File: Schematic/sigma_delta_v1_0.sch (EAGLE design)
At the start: 30 parts, among them Q1 BS170, Q2 BS170

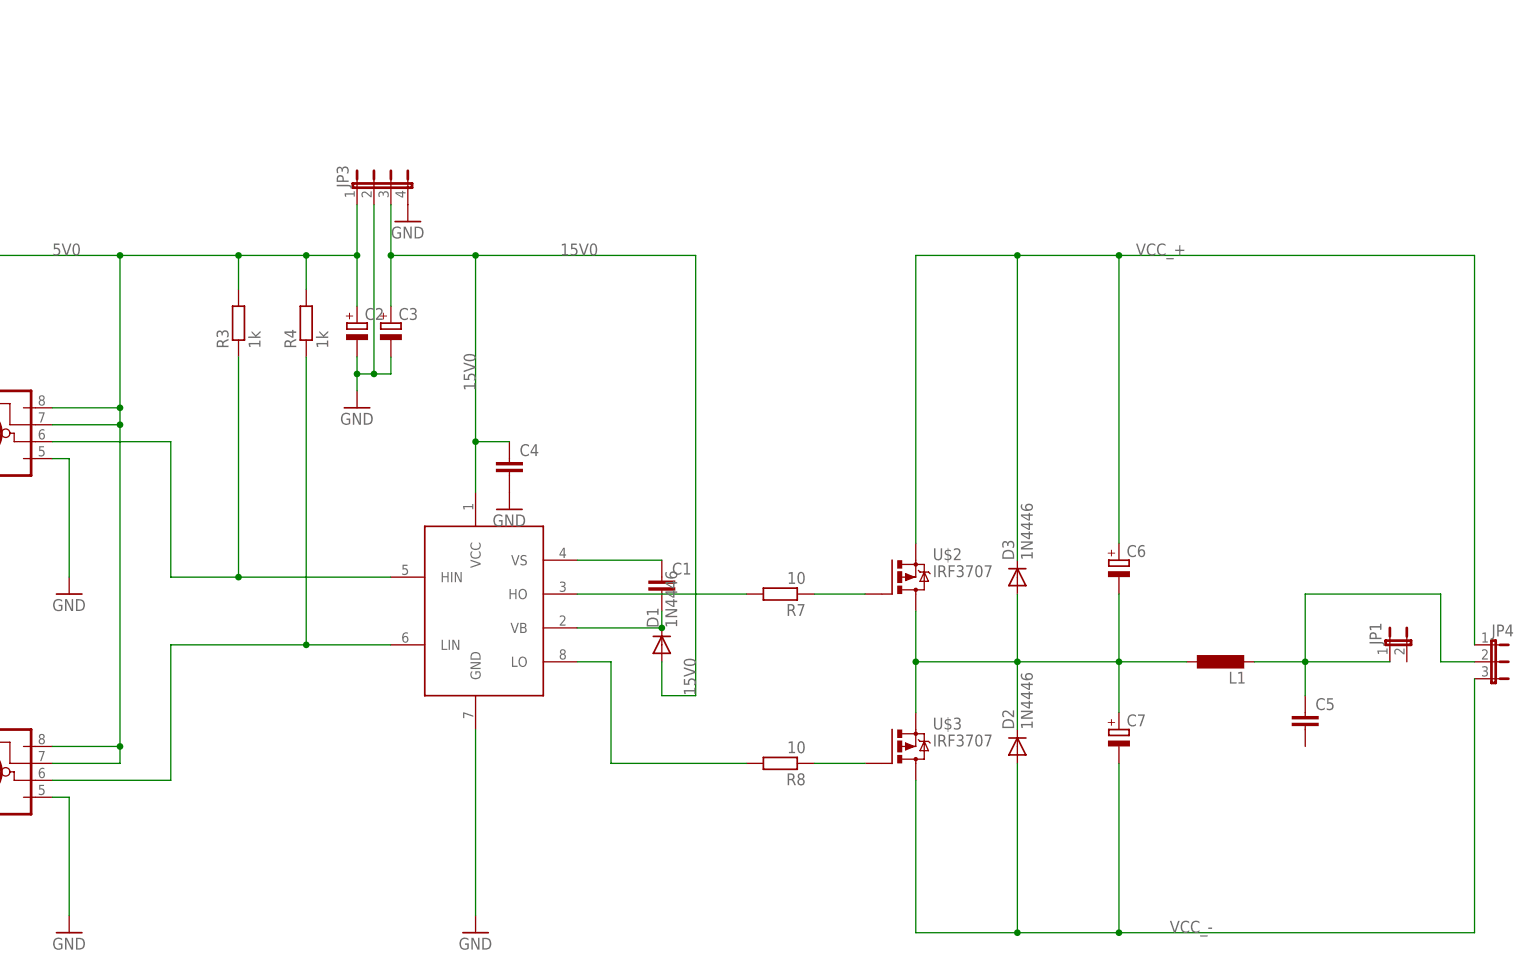
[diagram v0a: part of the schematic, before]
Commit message: first successfull stream of an audio file to the FPGA
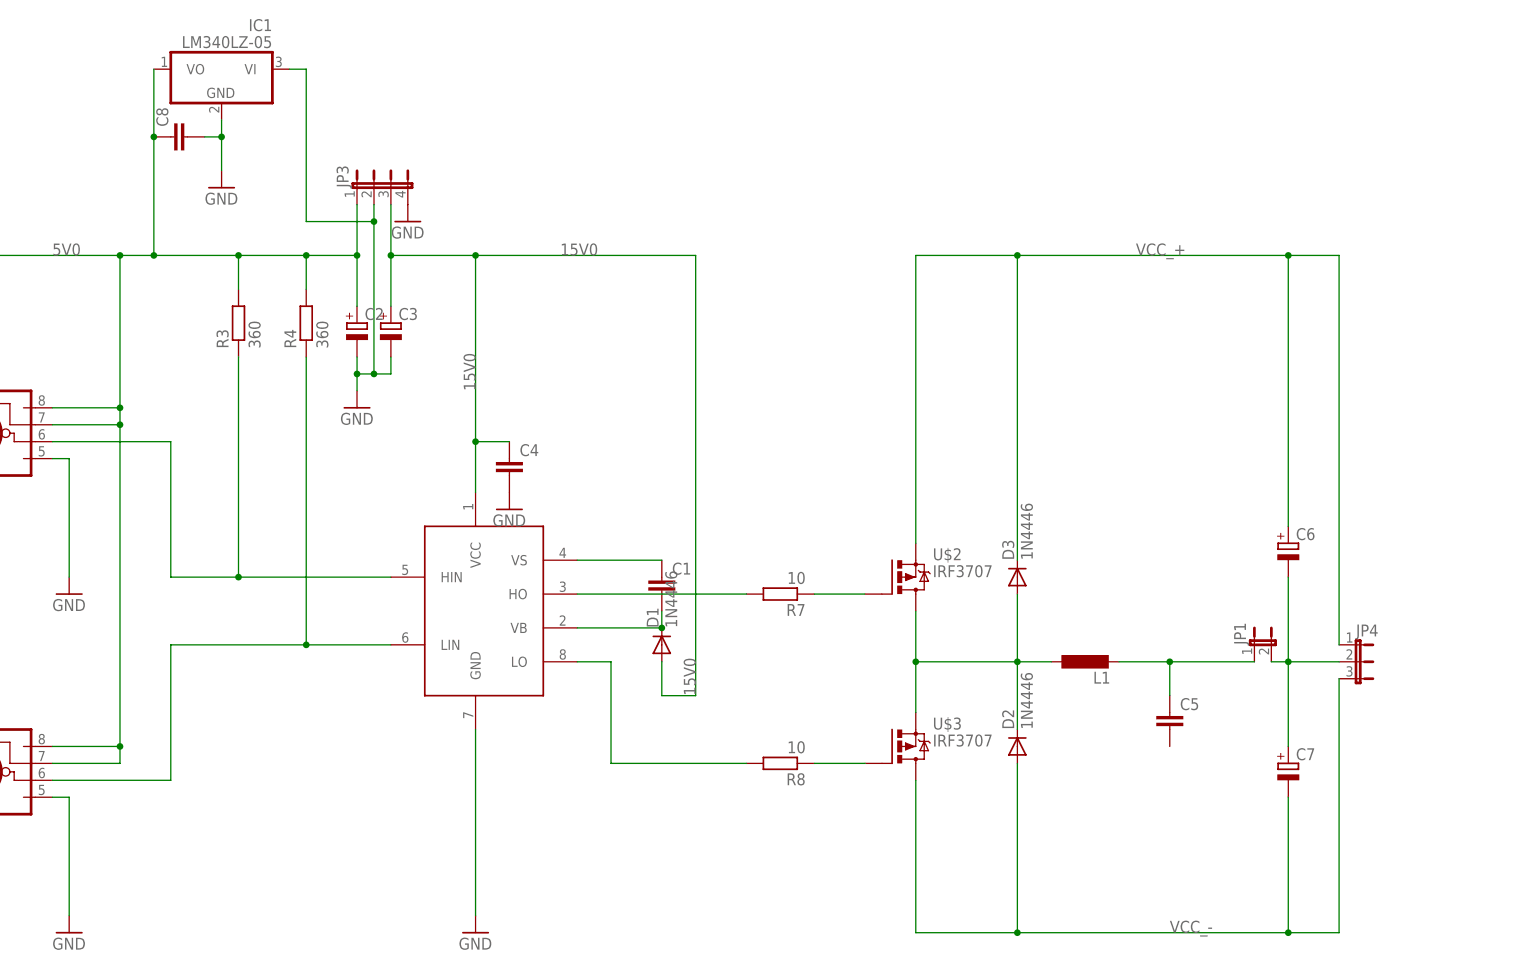
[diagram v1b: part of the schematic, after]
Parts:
- added C8: (no value), rcl:C-EU025-030X050
- added IC1: LM340LZ-05, linear:LM340LZ-05
- R3, R4: value 1k -> 360
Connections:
- new net N$19: C6.-, C7.+, JP1.2, JP4.2
- net 5V0: now also C8.1, IC1.VO
- net GND: now also C8.2, IC1.GND, IC1.VI
- net N$10: no longer JP4.2
- net N$9: no longer C6.-, C7.+
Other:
- moved on the sheet: C5, C6, C7, JP1, JP4, L1
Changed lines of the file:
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@@
 <part name="GND_5V0" library="supply1" deviceset="GND" device=""/>
 <part name="GND5" library="supply1" deviceset="GND" device=""/>
-<part name="R3" library="eagle-ltspice" deviceset="R" device="0207/10" value="1k"/>
-<part name="R4" library="eagle-ltspice" deviceset="R" device="0207/10" value="1k"/>
+<part name="R3" library="eagle-ltspice" deviceset="R" device="0207/10" value="360"/>
+<part name="R4" library="eagle-ltspice" deviceset="R" device="0207/10" value="360"/>
 <part name="GND6" library="supply1" deviceset="GND" device=""/>
 <part name="SUPPLY1" library="supply2" deviceset="GND" device="" value="F_GND"/>
@@
 <part name="D3" library="diode" deviceset="1N4446" device=""/>
 <part name="JP4" library="jumper" deviceset="JP2E" device=""/>
+<part name="IC1" library="linear" deviceset="LM340?-*" device="LZ" technology="05"/>
+<part name="GND4" library="supply1" deviceset="GND" device=""/>
+<part name="C8" library="rcl" deviceset="C-EU" device="025-030X050"/>
 </parts>
 <sheets>
@@
 <instance part="GND3" gate="1" x="147.32" y="182.88"/>
 <instance part="U$1" gate="G$1" x="147.32" y="167.64"/>
-<instance part="L1" gate="G$1" x="254" y="160.02" rot="R90"/>
-<instance part="C5" gate="G$1" x="266.7" y="152.4"/>
-<instance part="JP1" gate="A" x="279.4" y="162.56"/>
+<instance part="L1" gate="G$1" x="233.68" y="160.02" rot="R90"/>
+<instance part="C5" gate="G$1" x="246.38" y="152.4"/>
+<instance part="JP1" gate="A" x="259.08" y="162.56"/>
 <instance part="JP2" gate="G$1" x="20.32" y="175.26" rot="R90"/>
 <instance part="JP3" gate="G$1" x="127" y="231.14"/>
-<instance part="C6" gate="G$1" x="238.76" y="175.26"/>
-<instance part="C7" gate="G$1" x="238.76" y="149.86"/>
+<instance part="C6" gate="G$1" x="264.16" y="177.8"/>
+<instance part="C7" gate="G$1" x="264.16" y="144.78"/>
 <instance part="D2" gate="1" x="223.52" y="147.32" rot="R90"/>
 <instance part="D3" gate="1" x="223.52" y="172.72" rot="R90"/>
-<instance part="JP4" gate="1" x="294.64" y="160.02" rot="R270"/>
+<instance part="JP4" gate="1" x="274.32" y="160.02" rot="R270"/>
+<instance part="IC1" gate="A" x="104.14" y="248.92" rot="MR0"/>
+<instance part="GND4" gate="1" x="104.14" y="231.14"/>
+<instance part="C8" gate="G$1" x="96.52" y="238.76" rot="R90"/>
 </instances>
 <busses>
@@
 <wire x1="124.46" y1="200.66" x2="124.46" y2="203.2" width="0.1524" layer="91"/>
 <wire x1="124.46" y1="203.2" x2="124.46" y2="205.74" width="0.1524" layer="91"/>
-<wire x1="127" y1="228.6" x2="127" y2="203.2" width="0.1524" layer="91"/>
+<wire x1="127" y1="228.6" x2="127" y2="226.06" width="0.1524" layer="91"/>
+<wire x1="127" y1="226.06" x2="127" y2="203.2" width="0.1524" layer="91"/>
 <wire x1="127" y1="203.2" x2="124.46" y2="203.2" width="0.1524" layer="91"/>
 <junction x="124.46" y="203.2"/>
@@
 <junction x="127" y="203.2"/>
 <pinref part="JP3" gate="G$1" pin="2"/>
+<wire x1="127" y1="226.06" x2="116.84" y2="226.06" width="0.1524" layer="91"/>
+<wire x1="116.84" y1="226.06" x2="116.84" y2="248.92" width="0.1524" layer="91"/>
+<pinref part="IC1" gate="A" pin="VI"/>
+<wire x1="116.84" y1="248.92" x2="114.3" y2="248.92" width="0.1524" layer="91"/>
+<junction x="127" y="226.06"/>
 </segment>
 <segment>
@@
 <pinref part="GND2" gate="1" pin="GND"/>
 <pinref part="JP3" gate="G$1" pin="4"/>
+</segment>
+<segment>
+<pinref part="IC1" gate="A" pin="GND"/>
+<pinref part="GND4" gate="1" pin="GND"/>
+<wire x1="104.14" y1="233.68" x2="104.14" y2="238.76" width="0.1524" layer="91"/>
+<pinref part="C8" gate="G$1" pin="2"/>
+<wire x1="104.14" y1="238.76" x2="104.14" y2="241.3" width="0.1524" layer="91"/>
+<wire x1="101.6" y1="238.76" x2="104.14" y2="238.76" width="0.1524" layer="91"/>
+<junction x="104.14" y="238.76"/>
 </segment>
 </net>
@@
 <wire x1="48.26" y1="220.98" x2="55.88" y2="220.98" width="0.1524" layer="91"/>
 <wire x1="55.88" y1="220.98" x2="88.9" y2="220.98" width="0.1524" layer="91"/>
-<wire x1="88.9" y1="220.98" x2="106.68" y2="220.98" width="0.1524" layer="91"/>
+<wire x1="88.9" y1="220.98" x2="93.98" y2="220.98" width="0.1524" layer="91"/>
+<wire x1="93.98" y1="220.98" x2="106.68" y2="220.98" width="0.1524" layer="91"/>
 <wire x1="106.68" y1="220.98" x2="116.84" y2="220.98" width="0.1524" layer="91"/>
 <wire x1="116.84" y1="220.98" x2="116.84" y2="215.9" width="0.1524" layer="91"/>
@@
 <junction x="88.9" y="220.98"/>
 <pinref part="JP3" gate="G$1" pin="1"/>
+<pinref part="IC1" gate="A" pin="VO"/>
+<wire x1="93.98" y1="248.92" x2="93.98" y2="238.76" width="0.1524" layer="91"/>
+<junction x="93.98" y="220.98"/>
+<pinref part="C8" gate="G$1" pin="1"/>
+<wire x1="93.98" y1="238.76" x2="93.98" y2="220.98" width="0.1524" layer="91"/>
+<junction x="93.98" y="238.76"/>
 </segment>
 </net>
@@
 <pinref part="L1" gate="G$1" pin="1"/>
 <wire x1="208.28" y1="160.02" x2="208.28" y2="152.4" width="0.1524" layer="91"/>
-<wire x1="248.92" y1="160.02" x2="238.76" y2="160.02" width="0.1524" layer="91"/>
 <junction x="208.28" y="160.02"/>
-<pinref part="C6" gate="G$1" pin="-"/>
-<pinref part="C7" gate="G$1" pin="+"/>
-<wire x1="238.76" y1="160.02" x2="223.52" y2="160.02" width="0.1524" layer="91"/>
+<wire x1="228.6" y1="160.02" x2="223.52" y2="160.02" width="0.1524" layer="91"/>
 <wire x1="223.52" y1="160.02" x2="208.28" y2="160.02" width="0.1524" layer="91"/>
-<wire x1="238.76" y1="170.18" x2="238.76" y2="160.02" width="0.1524" layer="91"/>
-<junction x="238.76" y="160.02"/>
-<wire x1="238.76" y1="160.02" x2="238.76" y2="152.4" width="0.1524" layer="91"/>
 <pinref part="D2" gate="1" pin="C"/>
 <wire x1="223.52" y1="149.86" x2="223.52" y2="160.02" width="0.1524" layer="91"/>
@@
 <pinref part="L1" gate="G$1" pin="2"/>
 <pinref part="C5" gate="G$1" pin="1"/>
-<wire x1="259.08" y1="160.02" x2="266.7" y2="160.02" width="0.1524" layer="91"/>
-<wire x1="266.7" y1="160.02" x2="266.7" y2="154.94" width="0.1524" layer="91"/>
-<wire x1="266.7" y1="160.02" x2="279.4" y2="160.02" width="0.1524" layer="91"/>
+<wire x1="238.76" y1="160.02" x2="246.38" y2="160.02" width="0.1524" layer="91"/>
+<wire x1="246.38" y1="160.02" x2="246.38" y2="154.94" width="0.1524" layer="91"/>
+<wire x1="246.38" y1="160.02" x2="259.08" y2="160.02" width="0.1524" layer="91"/>
 <pinref part="JP1" gate="A" pin="1"/>
-<junction x="266.7" y="160.02"/>
-<wire x1="266.7" y1="160.02" x2="266.7" y2="170.18" width="0.1524" layer="91"/>
-<wire x1="266.7" y1="170.18" x2="287.02" y2="170.18" width="0.1524" layer="91"/>
-<wire x1="287.02" y1="170.18" x2="287.02" y2="160.02" width="0.1524" layer="91"/>
-<pinref part="JP4" gate="1" pin="2"/>
-<wire x1="287.02" y1="160.02" x2="292.1" y2="160.02" width="0.1524" layer="91"/>
+<junction x="246.38" y="160.02"/>
 </segment>
 </net>
@@
 <pinref part="JP4" gate="1" pin="1"/>
 <wire x1="208.28" y1="220.98" x2="223.52" y2="220.98" width="0.1524" layer="91"/>
-<wire x1="223.52" y1="220.98" x2="238.76" y2="220.98" width="0.1524" layer="91"/>
-<wire x1="238.76" y1="220.98" x2="292.1" y2="220.98" width="0.1524" layer="91"/>
-<wire x1="292.1" y1="220.98" x2="292.1" y2="162.56" width="0.1524" layer="91"/>
+<wire x1="223.52" y1="220.98" x2="264.16" y2="220.98" width="0.1524" layer="91"/>
+<wire x1="264.16" y1="220.98" x2="271.78" y2="220.98" width="0.1524" layer="91"/>
+<wire x1="271.78" y1="220.98" x2="271.78" y2="162.56" width="0.1524" layer="91"/>
 <label x="241.3" y="220.98" size="1.778" layer="95"/>
 <pinref part="D3" gate="1" pin="C"/>
 <wire x1="223.52" y1="175.26" x2="223.52" y2="220.98" width="0.1524" layer="91"/>
+<junction x="223.52" y="220.98"/>
 <pinref part="C6" gate="G$1" pin="+"/>
-<wire x1="238.76" y1="177.8" x2="238.76" y2="220.98" width="0.1524" layer="91"/>
-<junction x="223.52" y="220.98"/>
-<junction x="238.76" y="220.98"/>
+<wire x1="264.16" y1="180.34" x2="264.16" y2="220.98" width="0.1524" layer="91"/>
+<junction x="264.16" y="220.98"/>
 </segment>
 </net>
@@
 <pinref part="JP4" gate="1" pin="3"/>
 <wire x1="208.28" y1="119.38" x2="223.52" y2="119.38" width="0.1524" layer="91"/>
-<wire x1="223.52" y1="119.38" x2="238.76" y2="119.38" width="0.1524" layer="91"/>
-<wire x1="238.76" y1="119.38" x2="292.1" y2="119.38" width="0.1524" layer="91"/>
-<wire x1="292.1" y1="119.38" x2="292.1" y2="157.48" width="0.1524" layer="91"/>
+<wire x1="223.52" y1="119.38" x2="264.16" y2="119.38" width="0.1524" layer="91"/>
+<wire x1="264.16" y1="119.38" x2="271.78" y2="119.38" width="0.1524" layer="91"/>
+<wire x1="271.78" y1="119.38" x2="271.78" y2="157.48" width="0.1524" layer="91"/>
 <label x="246.38" y="119.38" size="1.778" layer="95"/>
 <pinref part="D2" gate="1" pin="A"/>
 <wire x1="223.52" y1="144.78" x2="223.52" y2="119.38" width="0.1524" layer="91"/>
+<junction x="223.52" y="119.38"/>
 <pinref part="C7" gate="G$1" pin="-"/>
-<wire x1="238.76" y1="144.78" x2="238.76" y2="119.38" width="0.1524" layer="91"/>
-<junction x="223.52" y="119.38"/>
-<junction x="238.76" y="119.38"/>
-</segment>
-</net>
+<wire x1="264.16" y1="139.7" x2="264.16" y2="119.38" width="0.1524" layer="91"/>
+<junction x="264.16" y="119.38"/>
+</segment>
+</net>
+<net name="N$19" class="0">
+<segment>
+<pinref part="C6" gate="G$1" pin="-"/>
+<pinref part="C7" gate="G$1" pin="+"/>
+<wire x1="264.16" y1="172.72" x2="264.16" y2="160.02" width="0.1524" layer="91"/>
+<pinref part="JP4" gate="1" pin="2"/>
+<wire x1="264.16" y1="160.02" x2="264.16" y2="147.32" width="0.1524" layer="91"/>
+<wire x1="271.78" y1="160.02" x2="264.16" y2="160.02" width="0.1524" layer="91"/>
+<pinref part="JP1" gate="A" pin="2"/>
+<wire x1="264.16" y1="160.02" x2="261.62" y2="160.02" width="0.1524" layer="91"/>
+<junction x="264.16" y="160.02"/>
+</segment>
+</net>

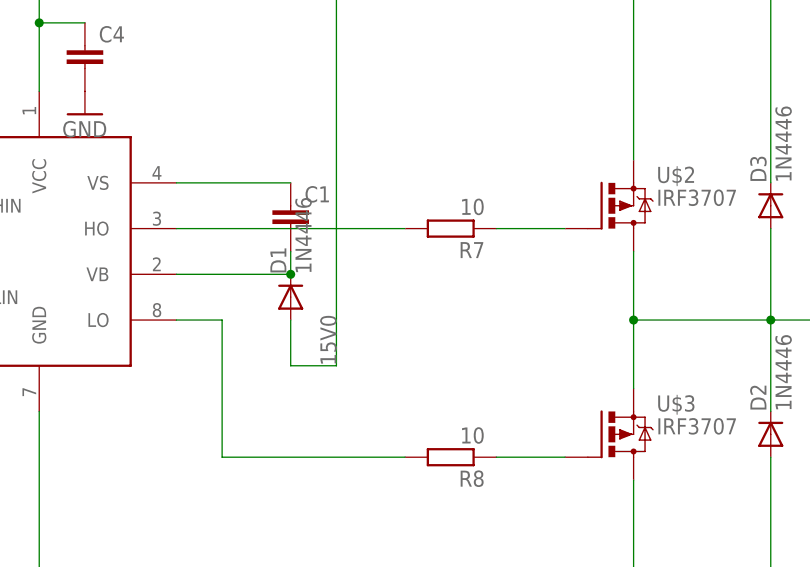
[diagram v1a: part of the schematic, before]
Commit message: added connection between VS and the Load within the scematic
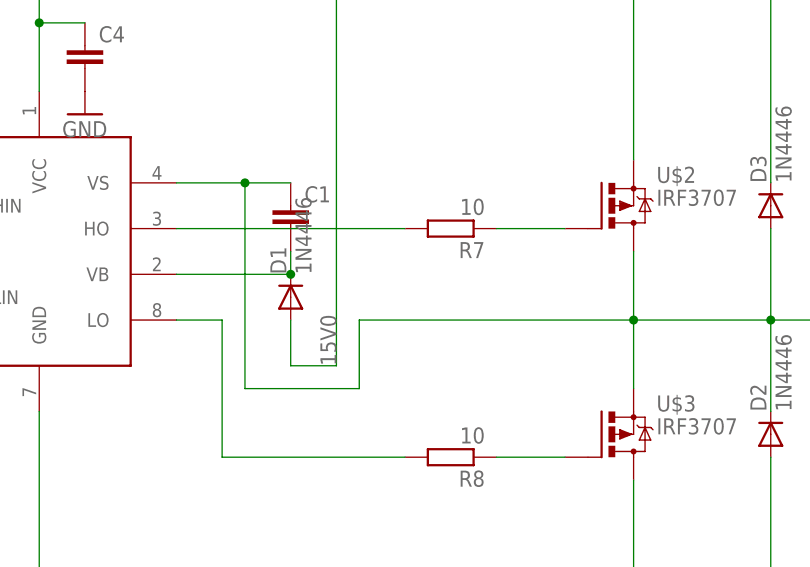
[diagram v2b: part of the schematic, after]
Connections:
- removed net N$18: C1.1, U$1.VS
- net N$9: now also C1.1, U$1.VS
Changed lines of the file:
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@@
-</segment>
-</net>
-<net name="N$18" class="0">
-<segment>
-<pinref part="C1" gate="G$1" pin="1"/>
-<wire x1="157.48" y1="175.26" x2="170.18" y2="175.26" width="0.1524" layer="91"/>
-<pinref part="U$1" gate="G$1" pin="VS"/>
 </segment>
 </net>
@@
 <wire x1="223.52" y1="160.02" x2="223.52" y2="170.18" width="0.1524" layer="91"/>
 <junction x="223.52" y="160.02"/>
+<wire x1="208.28" y1="160.02" x2="177.8" y2="160.02" width="0.1524" layer="91"/>
+<wire x1="177.8" y1="160.02" x2="177.8" y2="152.4" width="0.1524" layer="91"/>
+<pinref part="C1" gate="G$1" pin="1"/>
+<wire x1="157.48" y1="175.26" x2="165.1" y2="175.26" width="0.1524" layer="91"/>
+<pinref part="U$1" gate="G$1" pin="VS"/>
+<wire x1="165.1" y1="175.26" x2="170.18" y2="175.26" width="0.1524" layer="91"/>
+<wire x1="177.8" y1="152.4" x2="165.1" y2="152.4" width="0.1524" layer="91"/>
+<wire x1="165.1" y1="152.4" x2="165.1" y2="175.26" width="0.1524" layer="91"/>
+<junction x="165.1" y="175.26"/>
 </segment>
 </net>

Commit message: started reworking the scematic
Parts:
- removed C8: (no value), rcl:C-EU025-030X050
- removed JP1: (no value), jumper:JP1E
- removed JP3: (no value), jumper:JP4E
- removed JP4: (no value), jumper:JP2E
- added C10, C9: (no value), rcl:CPOL-EUE2.5-7
- added C11, C12: (no value), rcl:C-EUC0603
- added F1, F2: (no value), rcl:R-EU_M1206
- added IC2: MC78M12CDTG, linear:MC78M12CDTG
- added Q3, Q4: BSS84, transistor-small-signal:BSS84
- added R10, R11, R12, R9: 10K-100K, eagle-ltspice:RR0603
- added R13, R14: NP, eagle-ltspice:RR0603
- added X1: 1751251, con-phoenix-350:1751251
- added X2: 1751248, con-phoenix-350:1751248
- added X3: 1751264, con-phoenix-350:1751264
- C6, C7: device rcl:CPOL-EUE2.5-7 -> rcl:C-EUC0603
- IC1: value LM340LZ-05 -> MC78M12CDTG; device linear:LM340LZ-05 -> linear:MC78M12CDTG
- R1, R2, R3, R4, R5, R6, R7, R8: device eagle-ltspice:R0207/10 -> eagle-ltspice:RR0603
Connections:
- removed net 15V0: C3.+, C4.1, D1.A, JP3.3, U$1.VCC
- removed net 5V0: C2.+, C8.1, IC1.VO, JP3.1, OK1.VCC, OK1.VE, OK2.VCC, OK2.VE, R1.2, R2.2, R3.2, R4.2
- removed net N$8: OK2.VO, R4.1
- removed net VCC_+: C6.+, D3.C, JP4.1, U$2.S
- removed net VCC_-: C7.-, D2.A, JP4.3, U$3.D
- new net N$18: F1.2, X1-1.K
- new net N$20: F2.2, X1-2.K
- new net N$21: Q4.D, R14.2, U$1.LIN
- new net N$22: OK2.VO, Q4.G, R4.1
- new net VCC_12: C12.1, C2.+, C4.1, C6.1, D1.A, IC1.VI, IC2.VO, U$1.VCC
- new net VCC_3.3: C3.+, C7.1, IC1.VO, OK1.VCC, OK1.VE, OK2.VCC, OK2.VE, Q3.S, Q4.S, R3.2, R4.2
- new net VCC_FPGA: JP2.2, R1.2, R2.2, X3-2.K
- new net VCC_HI: C11.1, C9.+, D3.C, F1.1, IC2.VI, U$2.S
- new net VCC_MID: C10.+, C9.-, F2.1, X2-1.K
- net GND: now also C10.-, C11.2, C12.2, C5.2, C6.2, C7.2, D2.A, IC2.GND, JP2.1, R10.2, R11.2, R12.2, R13.1, R14.1, U$3.D, X1-3.K, X3-1.K; no longer C8.2, IC1.VI, JP2.2, JP2.3, JP3.2, JP3.4
- net N$1: now also X3-4.K
- net N$10: now also X2-2.K; no longer JP1.1
- net N$11: now also R11.1
- net N$12: now also R12.1
- net N$14: now also R9.1
- net N$15: now also R10.1
- net N$19: now also Q3.D, R13.2, U$1.HIN; no longer C6.-, C7.+, JP1.2, JP4.2
- net N$2: now also JP2.3, X3-3.K; no longer JP2.1
- net N$6: now also R2.1
- net N$7: now also Q3.G; no longer U$1.HIN
- net N$9: now also R9.2
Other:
- note added: "Should be in one package or matched!"
- moved on the sheet: C1, C2, C3, C4, C5, D1, D2, D3, JP2, L1, OK1, OK2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
